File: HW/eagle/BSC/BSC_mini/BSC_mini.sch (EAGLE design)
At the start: 397 parts, among them IC1101 50MHz, IC1201 XC2C384-10TQG144C, IC1301 MAX517ACSA+, IC1302 MAX517ACSA+, IC1401 MAX962ESA+, IC1801 4093N, IC2001 4093N, IC201 LM1117T-ADJ, IC202 LM1117T-ADJ, IC203 LM1117T-ADJ, IC204 LM1117T-ADJ, IC205 LM1117T-ADJ, IC301 LM1117T-ADJ, IC302 LM1117T-ADJ, IC401 4093N, IC601 AS6C4008-55PCN, IC602 AS6C4008-55PCN, IC603 AS6C4008-55PCN, IC701 AM29LV040B, IC702 24LC256-I/SN, IC801 XC3S400-4PQG208C, IC802 XCF04SVOG20C, J1201 JUMPER_1X2-T-VERTICAL_GRID_2.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, J501 JUMPER_1X2-T-VERTICAL_GRID_2.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, J801 JUMPER_2X10-T-VERTICAL, T1901 DMG3420U, T1902 DMG3420U, T2101 DMG3420U, T2102 DMG3420U, T2103 DMG3420U, T2104 DMG3420U, T2105 DMG3420U, T2106 DMG3420U, T2107 DMG3420U, T2108 DMG3420U, T2109 DMG3420U, T2110 DMG3420U, T2201 DMG3420U, T2202 DMG3420U, T2203 DMG3420U, T2204 DMG3420U, T2301 DMG3420U, T2302 DMG3420U, T2303 DMG3420U, T2304 DMG3420U, T2305 DMG3420U, T2306 DMG3420U, T2307 DMG3420U, T2308 DMG3420U, T2401 NX2301P, T2402 NX2301P, T2403 NX2301P, T2404 NX2301P, T2405 NX2301P, T2406 NX2301P, T2407 DMG3420U, T2408 DMG3420U, T2501 NX2301P, T2502 NX2301P, T2503 NX2301P, T2504 NX2301P, T2505 NX2301P, T2506 NX2301P, T2507 DMG3420U, T2508 DMG3420U, T301 DMG3420U, T302 DMG3420U, T303 DMG3420U, T304 DMG3420U, T305 DMG3420U, T306 DMG3420U, T401 DMG3420U, X101 CLAMP_1X2-T-2.5MM, X102 MALE_2X5-T-VERTICAL_2MM54, X103 MALE_1X3, X104 MALE_2X13-T-VERTICAL_PITCH_2M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, X105 MALE_1X3, X106 MALE_2X13-T-VERTICAL_PITCH_2M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, X107 MALE_1X3, X1201 MALE_2X5-T-VERTICAL_2MM54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

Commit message: voltages on testpoints
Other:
- note added: "120..160mA wenn 1,25V jumper geschlossen"
- note added: "P3V3 when J301 open"
- note added: "P3V3 when J302 open"
- note removed: "120mA wenn 1,25V jumper geschlossen"
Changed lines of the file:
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@@
 <text x="403.86" y="353.06" size="1.27" layer="97" font="fixed">45mA alle Jumper offen</text>
 <text x="403.86" y="322.58" size="1.27" layer="97" font="fixed">450mA alle Spannungsregler jumper zu</text>
-<text x="403.86" y="342.9" size="1.27" layer="97" font="fixed">120mA wenn 1,25V jumper geschlossen</text>
+<text x="403.86" y="342.9" size="1.27" layer="97" font="fixed">120..160mA wenn 1,25V jumper geschlossen</text>
 <text x="403.86" y="347.98" size="1.27" layer="97" font="fixed">inbetriebname:</text>
 <text x="403.86" y="345.44" size="1.27" layer="97" font="fixed">-----------------------------------</text>
@@
 <text x="149.86" y="35.56" size="1.27" layer="91" font="fixed">invalid ?</text>
 <text x="71.12" y="152.4" size="1.27" layer="97" font="fixed">5.2mA</text>
+<text x="66.04" y="165.1" size="1.778" layer="97" font="fixed">P3V3 when J301 open</text>
+<text x="190.5" y="165.1" size="1.778" layer="97" font="fixed">P3V3 when J302 open</text>
 </plain>
 <instances>

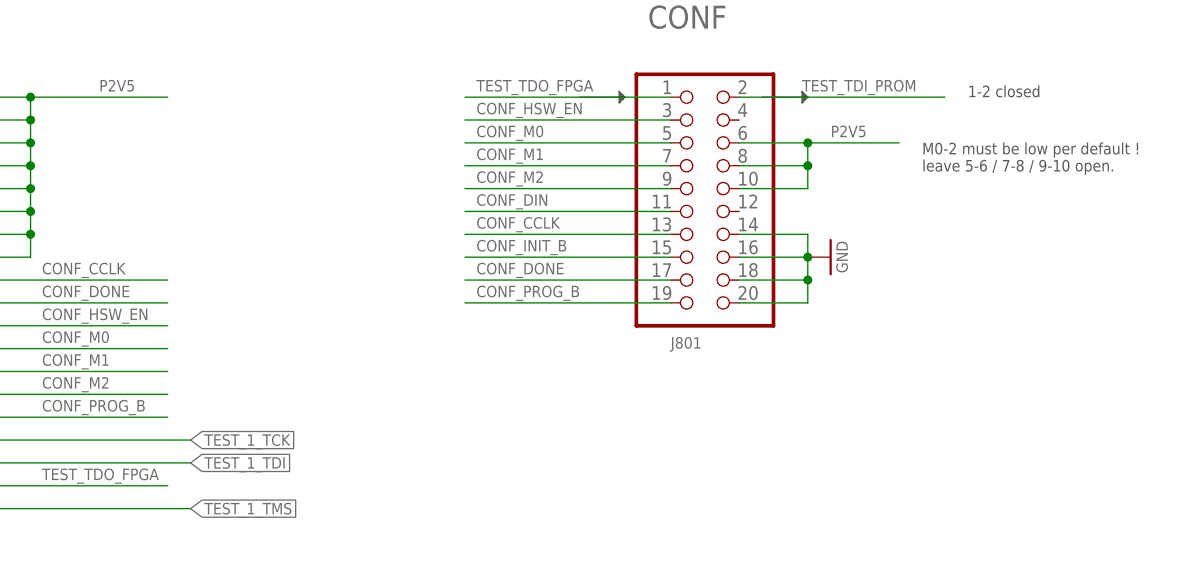
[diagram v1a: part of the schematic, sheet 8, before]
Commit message: notes on BST mode
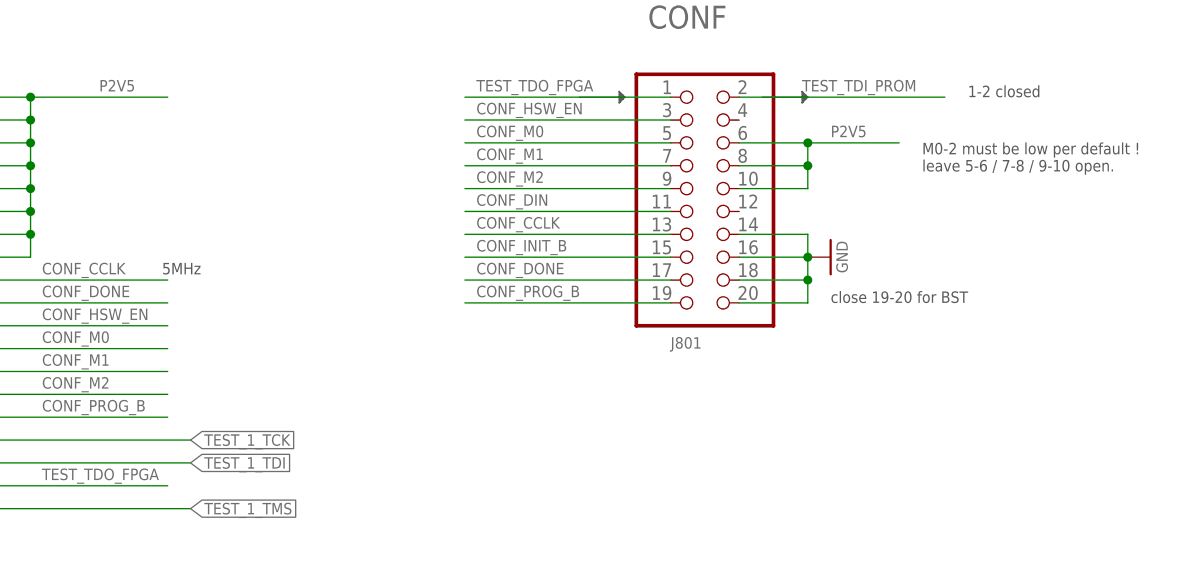
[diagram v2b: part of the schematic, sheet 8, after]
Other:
- note added: "5MHz"
- note added: "close 19-20 for BST"
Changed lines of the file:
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@@
 leave 5-6 / 7-8 / 9-10 open.</text>
 <text x="154.94" y="157.48" size="1.27" layer="97" font="fixed">1-2 closed</text>
+<text x="139.7" y="134.62" size="1.27" layer="97" font="fixed">close 19-20 for BST</text>
+<text x="65.405" y="137.795" size="1.27" layer="97" font="fixed">5MHz</text>
 </plain>
 <instances>
